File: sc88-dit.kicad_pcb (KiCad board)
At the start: 2 copper layers, 70 x 51 mm, 70 parts, among them J1 Conn_01x04_Male, J2 Conn_01x04_Male, J3 Conn_01x06_Male, J4 Conn_01x06_Male, U1 74LVC1G74, U2 AK4103A

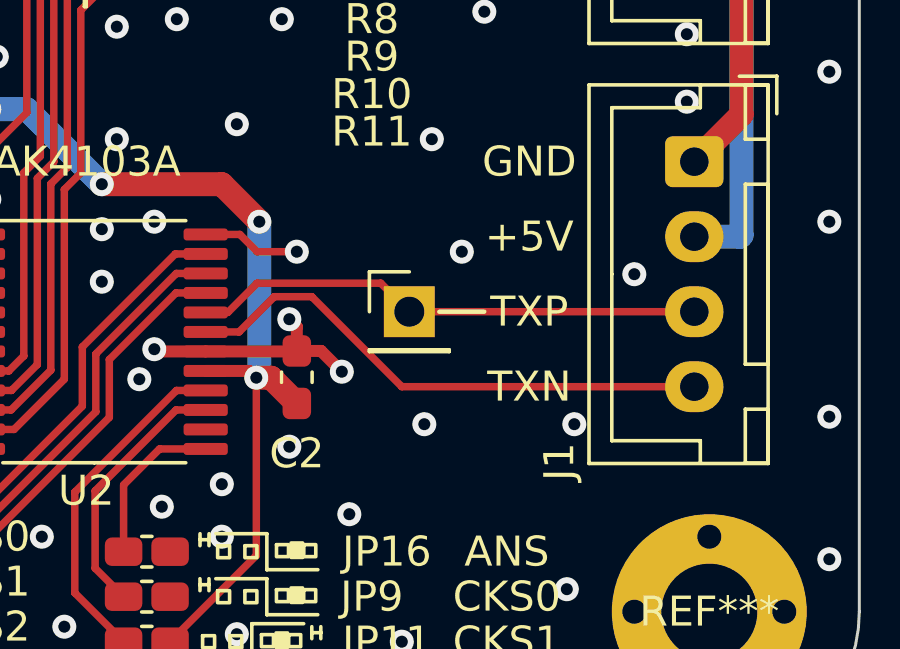
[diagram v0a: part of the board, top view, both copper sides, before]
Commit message: Added TXP/TXN jumper(or resistor)
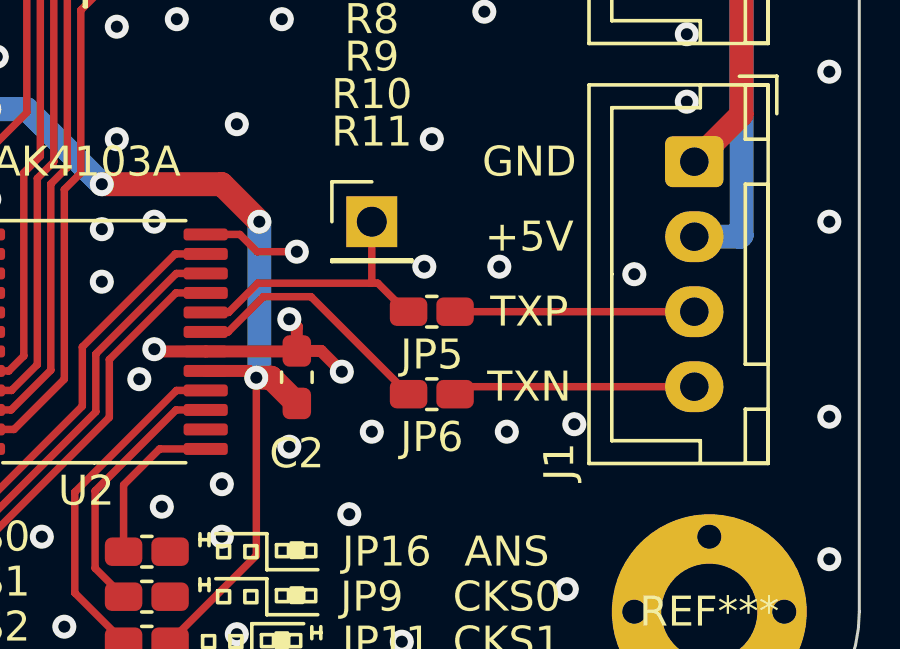
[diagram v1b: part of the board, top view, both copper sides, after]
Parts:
- added JP5: Jumper_NO_Small, components:R_0603_1608Metric_SolderJumperCompatible, F.Cu at (72.8, 116.0)
- added JP6: Jumper_NO_Small, components:R_0603_1608Metric_SolderJumperCompatible, F.Cu at (72.8, 118.8)
- moved TP4 3.25 mm to (70.8, 113.0)
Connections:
- J1 pad 3: /TXP -> Net-(J1-Pad3)
- J1 pad 4: /TXN -> Net-(J1-Pad4)
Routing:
- net /TXN: track 18.0 -> 8.60 mm
- net Net-(J1-Pad4): track 0.00 -> 8.08 mm
- net Net-(J1-Pad3): track 0.00 -> 7.97 mm
- net /TXP: track 17.1 -> 9.63 mm
- net GND: vias 191 -> 193

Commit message: Relocated freq. divider to make traces simple
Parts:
- moved C4 7.78 mm to (54.8, 105.8), turned to 180 degrees
- moved R1 6.93 mm to (54.8, 104.0), turned to 0 degrees
- moved TP1 6.27 mm to (54.0, 109.8)
- moved U1 5.32 mm to (49.8, 103.0)
- moved C1 5.00 mm to (51.2, 100.2)
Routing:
- net +5V: track 135.6 -> 123.1 mm, vias 10 -> 4
- net /HALF_MCLK: track 26.4 -> 19.4 mm
- net /MCLK: track 32.9 -> 27.8 mm
- net Net-(R1-Pad1): track 5.82 -> 2.44 mm
- net GND: track 71.4 -> 72.9 mm, vias 193 -> 188
